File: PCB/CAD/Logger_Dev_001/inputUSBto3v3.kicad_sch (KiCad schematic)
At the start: 3 parts, among them J2 2171750001, U1 NCP1117-5.0_SOT223, U4 MCP2221AxSL

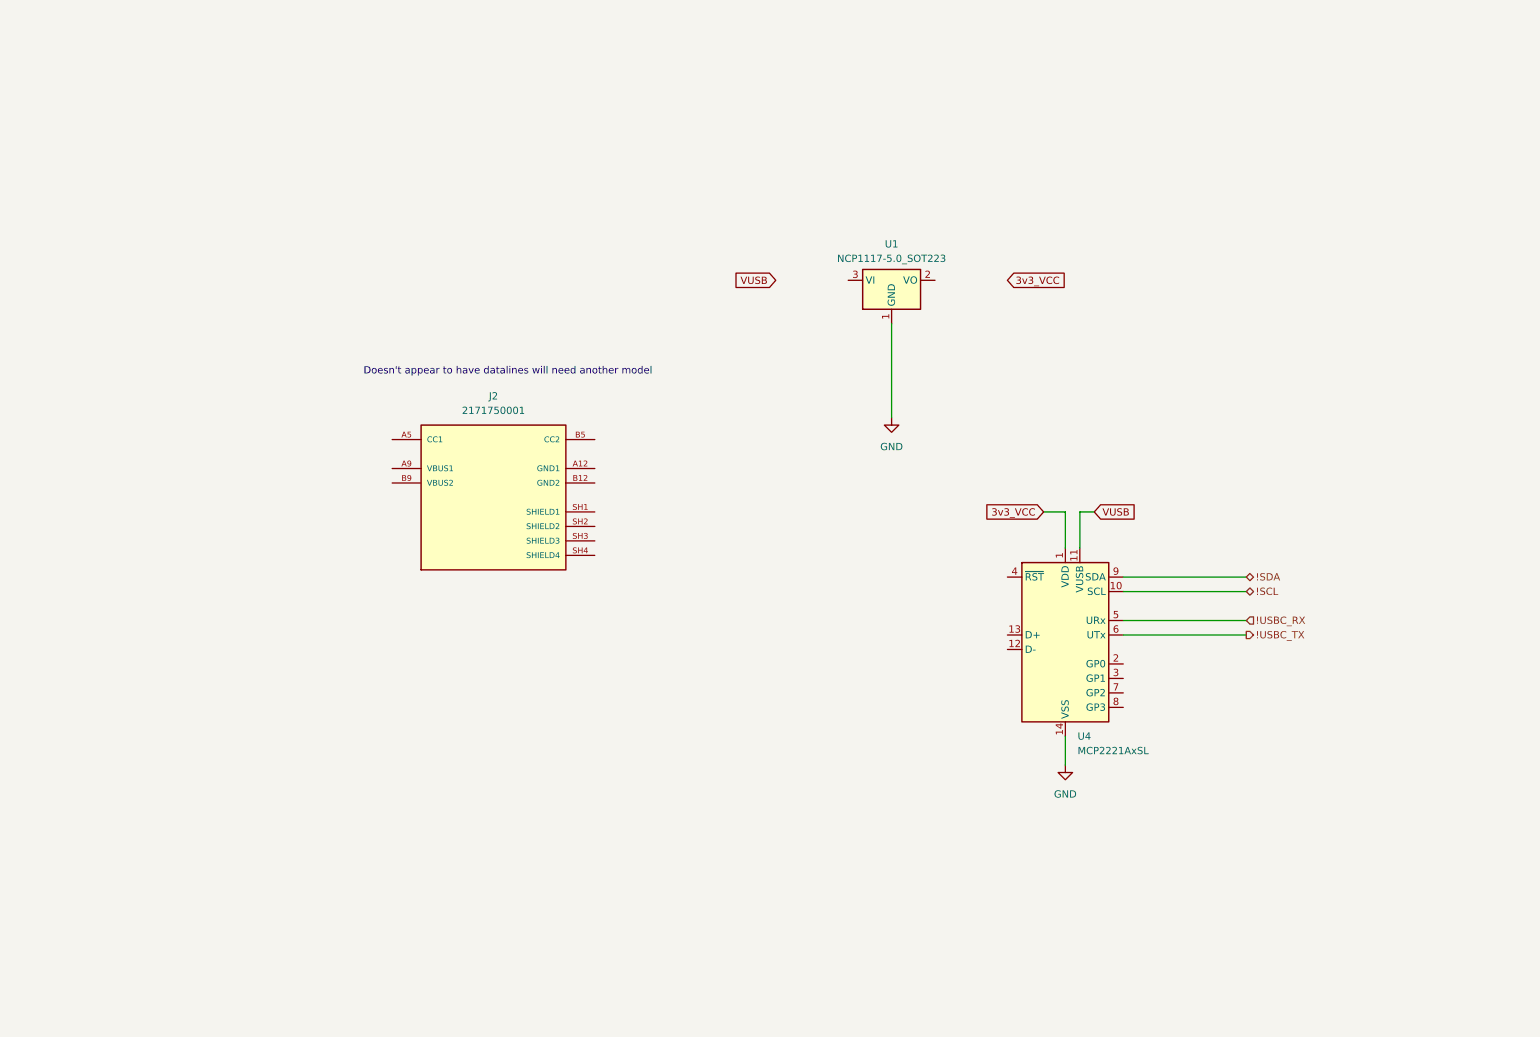
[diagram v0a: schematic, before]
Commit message: JLCPCB Component Updates
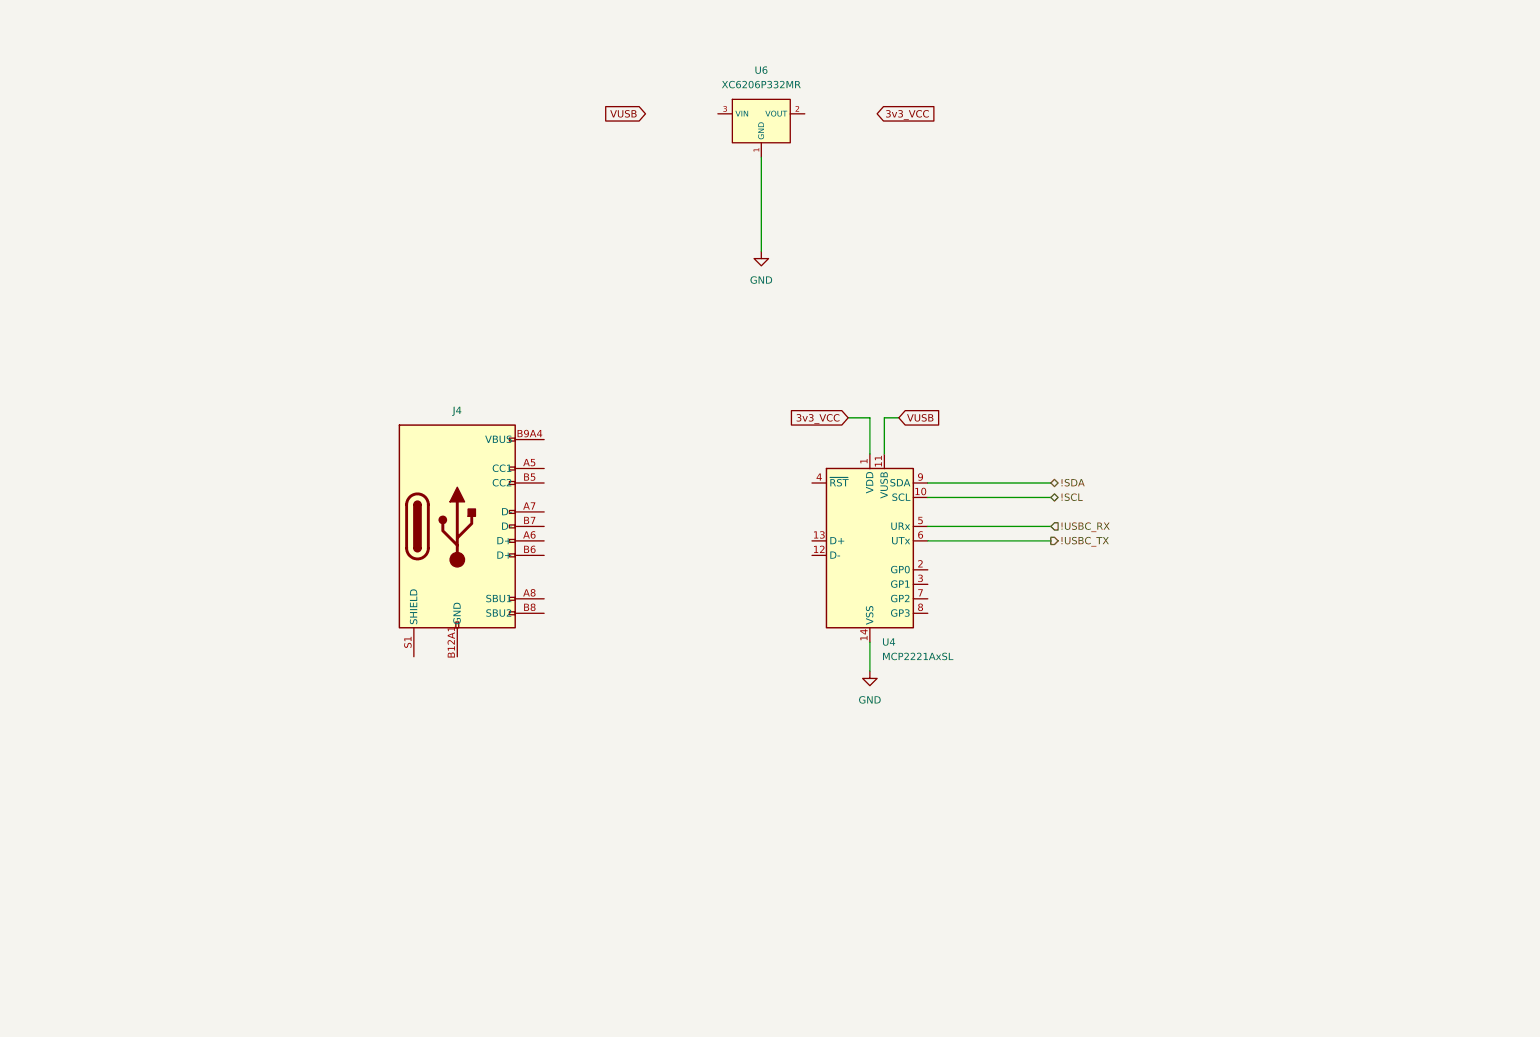
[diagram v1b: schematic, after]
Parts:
- removed J2: 2171750001, 2171750001:MOLEX_2171750001, symbol 2171750001:2171750001
- removed U1: NCP1117-5.0_SOT223, Package_TO_SOT_SMD:SOT-223-3_TabPin2, symbol Regulator_Linear:NCP1117-5.0_SOT223
- added J4: Connector, USB-TYPE-C-16P, PCM_JLCPCB:TYPE-C-SMD_HX-TYPE-C-16PIN, symbol PCM_JLCPCB-Extended:Connector, USB-TYPE-C-16P
- added U6: XC6206P332MR, PCM_JLCPCB:SOT-23-3_L2.9-W1.6-P1.90-LS2.8-BR, symbol PCM_JLCPCB-Power:LDO, 3.3V, 0.2A
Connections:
- net GND: now also U6.1 (GND)
- new net: J4.A12B1 (GND), J4.B12A1 (GND)
- new net: J4.A9B4 (VBUS), J4.B9A4 (VBUS)
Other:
- note removed: "Doesn't appear to have datalines will need another model"
- moved on the sheet: U4

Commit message: Library Submodule Update
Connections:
- net GND: now also J4.A12B1 (GND), J4.B12A1 (GND), J4.S1 (SHIELD)
- net at J4.A6 (D+): now also J4.B6 (D+), U4.13 (D+)
- net at J4.A7 (D-): now also J4.B7 (D-), U4.12 (D-)
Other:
- moved on the sheet: J4

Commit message: Update kicad project
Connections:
- net VUSB: now also J4.A9B4 (VBUS), J4.B9A4 (VBUS)
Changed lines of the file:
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@@
+	(wire
+		(pts
+			(xy 109.22 77.47) (xy 109.22 88.9)
+		)
+		(stroke
+			(width 0)
+			(type default)
+		)
+	)
 	(wire
 		(pts
@@
 		(pts
 			(xy 198.12 100.33) (xy 176.53 100.33)
+		)
+		(stroke
+			(width 0)
+			(type default)
+		)
+	)
+	(wire
+		(pts
+			(xy 118.11 77.47) (xy 109.22 77.47)
 		)
 		(stroke
@@
 				(hide yes)
 			)
+		)
+	)
+	(global_label "VUSB"
+		(shape input)
+		(at 118.11 77.47 0)
+		(fields_autoplaced yes)
+		(effects
+			(font
+				(size 1.27 1.27)
+			)
+			(justify left)
+		)
+		(property "Intersheetrefs" "${INTERSHEET_REFS}"
+			(at 125.9938 77.47 0)
+			(effects
+				(font
+					(size 1.27 1.27)
+				)
+				(justify left)
+				(hide yes)
+			)

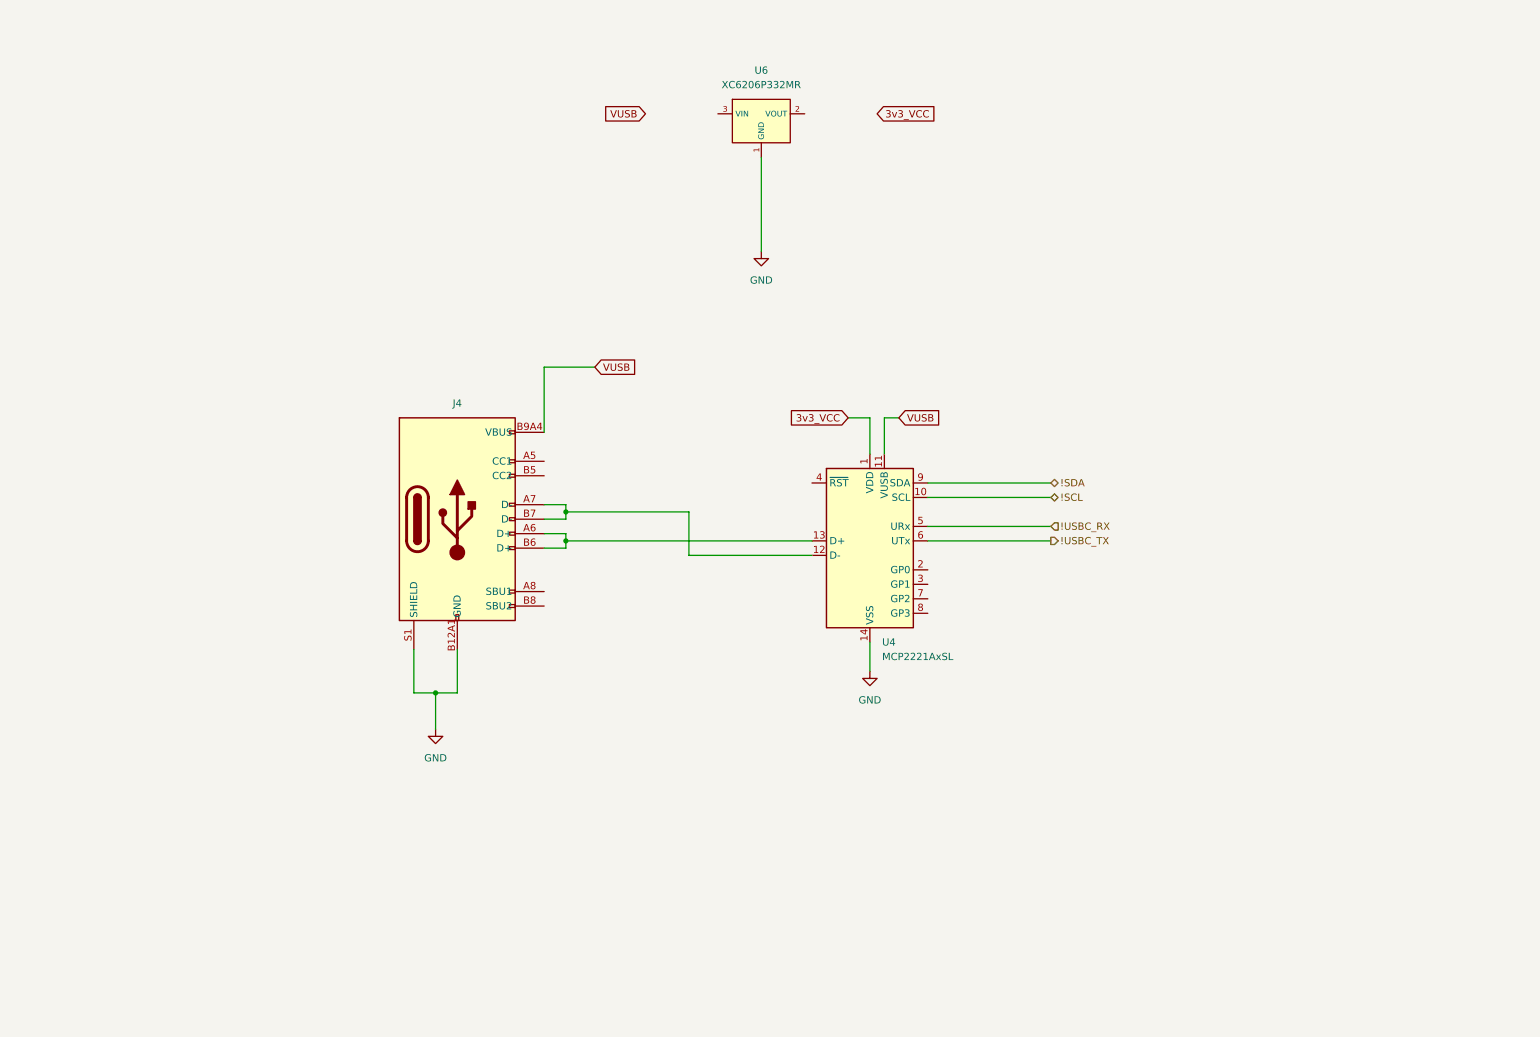
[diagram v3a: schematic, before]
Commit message: USB Passive Component updates
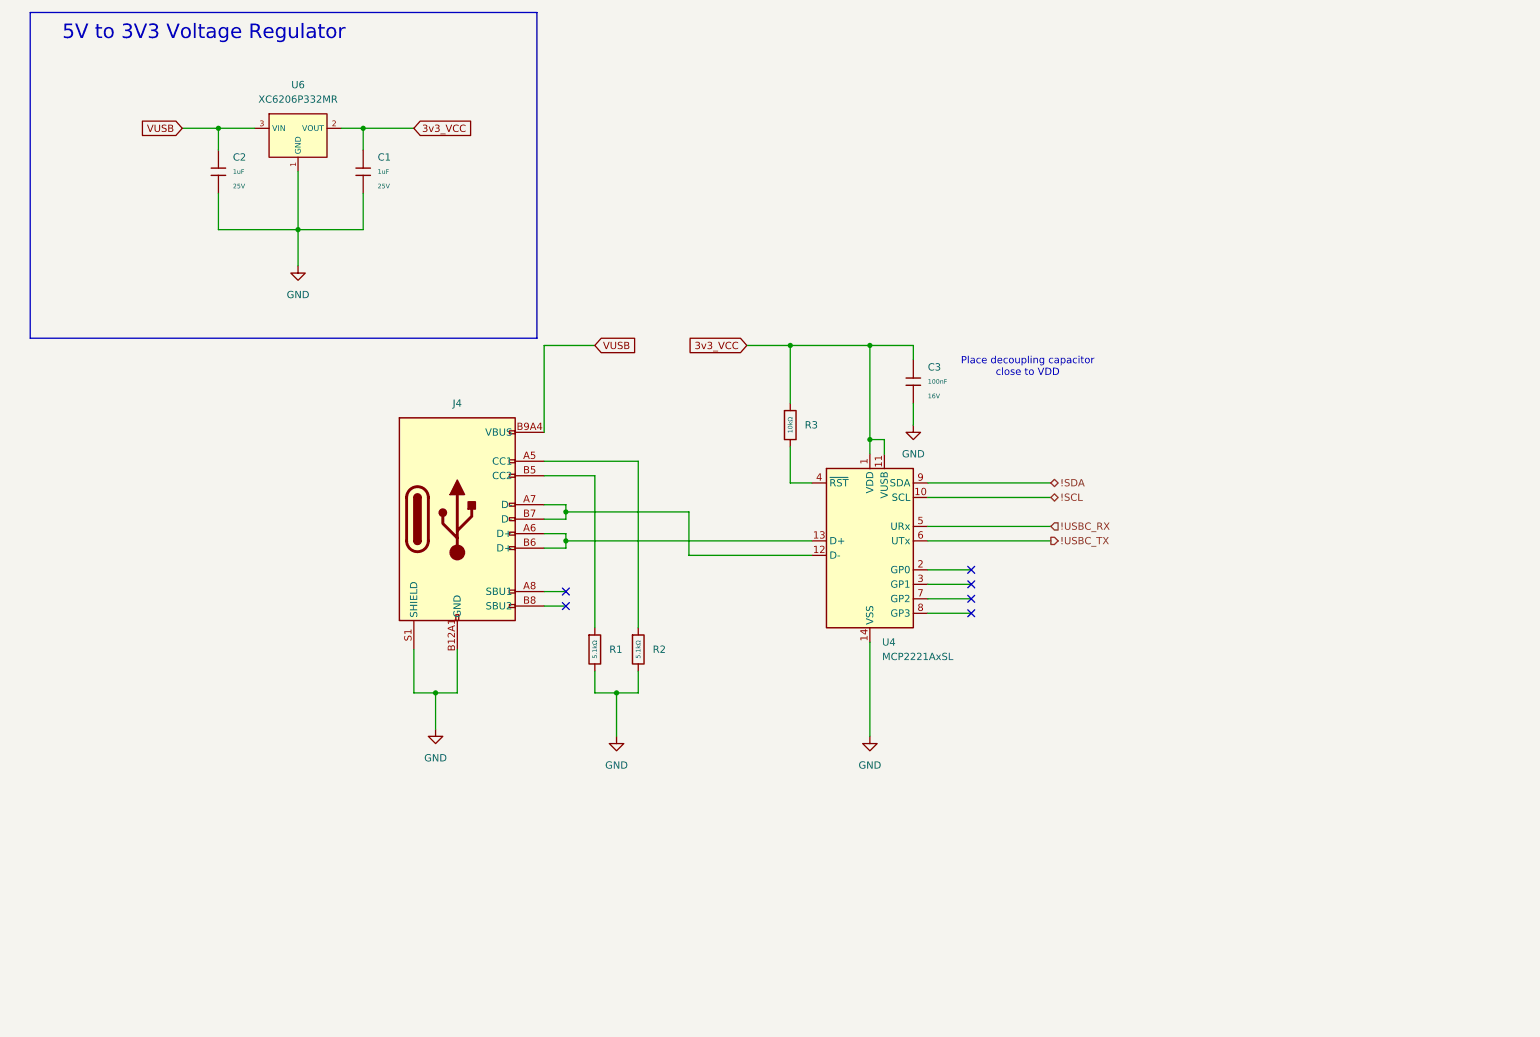
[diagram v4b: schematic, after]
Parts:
- added C1, C2: 1uF, PCM_JLCPCB:C_0402, symbol PCM_JLCPCB-Capacitors:0402,1uF
- added C3: 100nF, PCM_JLCPCB:C_0402, symbol PCM_JLCPCB-Capacitors:0402,100nF
- added R1, R2: 5.1kΩ, PCM_JLCPCB:R_0402, symbol PCM_JLCPCB-Resistors:0402,5.1kΩ
- added R3: 10kΩ, PCM_JLCPCB:R_0402, symbol PCM_JLCPCB-Resistors:0402,10kΩ
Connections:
- net 3v3_VCC: now also U4.11 (VUSB), U6.2 (VOUT), C1.1, C3.1, R3.1
- net GND: now also C1.2, C2.2, C3.2, R1.2, R2.2
- net VUSB: now also U6.3 (VIN), C2.1; no longer U4.11 (VUSB)
- net at J4.A5 (CC1): now also R2.1
- net at J4.B5 (CC2): now also R1.1
- net at U4.4 (~{RST}): now also R3.2
- no-connect marks 0 -> 6
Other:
- note added: "5V to 3V3 Voltage Regulator"
- note added: "Place decoupling capacitor close to VDD"
- moved on the sheet: U6

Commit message: Power input Schematic
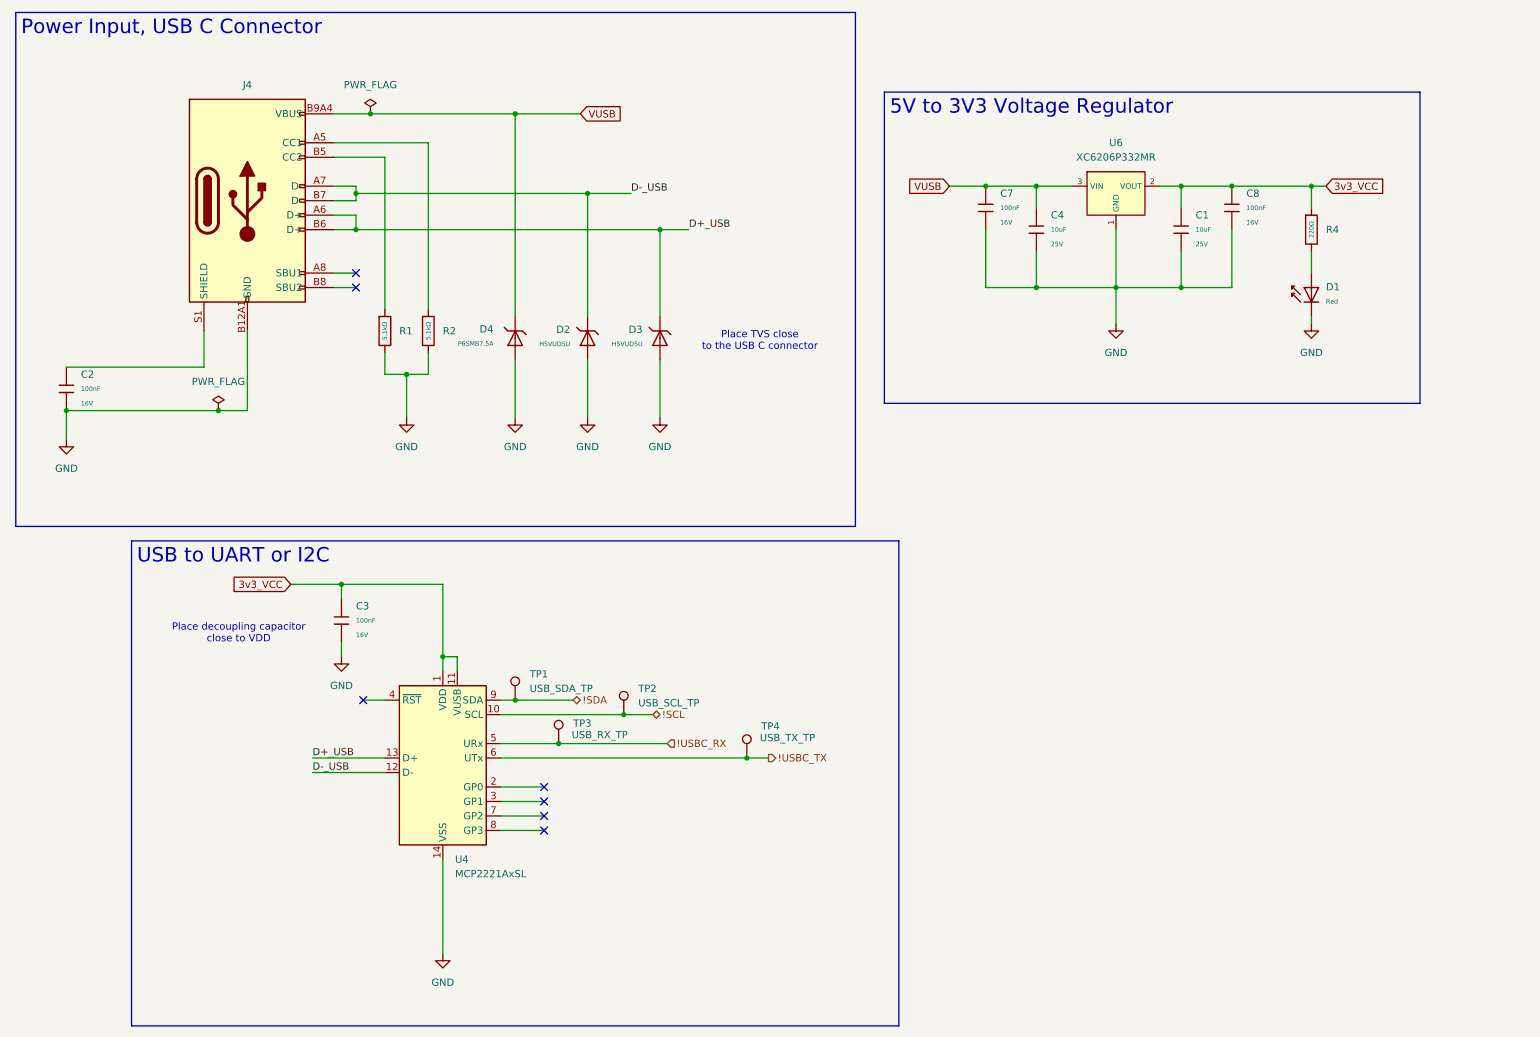
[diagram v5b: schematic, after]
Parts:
- removed C1, C2: 1uF, PCM_JLCPCB:C_0402, symbol PCM_JLCPCB-Capacitors:0402,1uF
- removed R3: 10kΩ, PCM_JLCPCB:R_0402, symbol PCM_JLCPCB-Resistors:0402,10kΩ
- added C1, C4: 10uF, PCM_JLCPCB:C_0603, symbol PCM_JLCPCB-Capacitors:0603,10uF,(2)
- added C2, C7, C8: 100nF, PCM_JLCPCB:C_0402, symbol PCM_JLCPCB-Capacitors:0402,100nF
- added D1: Red, PCM_JLCPCB:D_0805, symbol PCM_JLCPCB-Diodes:LED,0805,Red
- added D2, D3: H5VUD5U, PCM_JLCPCB:D_SOD-523, symbol PCM_JLCPCB-Diodes:TVS-Uni,H5VUD5U
- added D4: P6SMB7.5A, PCM_JLCPCB:D_SMB, symbol PCM_JLCPCB-Diodes:TVS-Uni,P6SMB7.5A
- added R4: 220Ω, PCM_JLCPCB:R_0402, symbol PCM_JLCPCB-Resistors:0402,220Ω
- added TP1: USB_SDA_TP, symbol Connector:TestPoint
- added TP2: USB_SCL_TP, symbol Connector:TestPoint
- added TP3: USB_RX_TP, symbol Connector:TestPoint
- added TP4: USB_TX_TP, symbol Connector:TestPoint
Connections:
- net !SCL: now also TP2.1
- net !SDA: now also TP1.1
- net !USBC_RX: now also TP3.1
- net !USBC_TX: now also TP4.1
- net 3v3_VCC: now also C1.1, C8.1, R4.1
- net GND: now also C1.2, C2.2, C4.2, C7.2, C8.2, D1.1, D2.2, D3.2, D4.2; no longer J4.S1 (SHIELD)
- net VUSB: now also C4.1, C7.1, D4.1
- net D+_USB: now reaches J4.A6 (D+), J4.B6 (D+), U4.13 (D+)
- net D+_USB: now also D3.1
- net D-_USB: now reaches J4.A7 (D-), J4.B7 (D-), U4.12 (D-)
- net D-_USB: now also D2.1
- new net: C2.1, J4.S1 (SHIELD)
- new net: D1.2, R4.2
- no-connect marks 6 -> 7
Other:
- note added: "Place TVS close to the USB C connector"
- note removed: "5V to 3V3 Voltage Regulator"
- moved on the sheet: C3, J4, R1, R2, U4, U6
